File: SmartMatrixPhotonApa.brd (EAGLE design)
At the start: 40.6 x 35.6 mm, 13 parts, among them IC2 74AHC1G08DBV, IC3 74AHC1G08DBV, J1 0-DNP, U1 microSD

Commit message: Rough routing of board, not close to passing DRC
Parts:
- moved C1 7.38 mm to (18.3, 15.0)
- moved JP6 6.97 mm to (20.3, 18.3), turned to 180 degrees
- moved JP8 6.97 mm to (20.3, 18.3)
- moved C2 6.91 mm to (15.7, 18.3), turned to 90 degrees
- moved D1 6.43 mm to (15.2, 11.7)
- moved IC2 6.43 mm to (22.6, 11.4)
- moved IC3 6.43 mm to (18.5, 11.4)
- moved JP3 6.43 mm to (10.4, 0.00)
- moved R2 6.43 mm to (25.7, 11.2)
- moved U1 6.43 mm to (27.6, 20.3)
- moved JP1 6.43 mm to (20.6, 7.62)
- moved J1 5.39 mm to (24.6, 16.5)
- moved R1 4.49 mm to (24.6, 18.5), turned to 0 degrees
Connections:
- net V3.3 renamed 3V3
- new net N$1: JP3.GND@0, JP3.GND@0_1, JP3.GND@0_2, JP3.GND@0_S1, JP3.GND@0_S2
- net GND: now also JP3.GND@2, JP3.GND@2_1, JP3.GND@2_2, JP3.GND@2_S1, JP3.GND@2_S2; no longer JP3.GND@0, JP3.GND@0_1, JP3.GND@0_2, JP3.GND@0_S1, JP3.GND@0_S2
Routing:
- net GND: track 0.00 -> 77.4 mm, vias 0 -> 2
- net VIN: track 0.00 -> 45.6 mm
- net SPI_SCK: track 0.00 -> 26.6 mm, vias 0 -> 1
- net SD_CS: track 0.00 -> 25.9 mm, vias 0 -> 1
- net SPI_MISO: track 0.00 -> 25.4 mm, vias 0 -> 1
- net 3V3: track 0.00 -> 23.9 mm, vias 0 -> 1
- net SPI_MOSI: track 0.00 -> 21.6 mm, vias 0 -> 1
- net N$4: track 0.00 -> 17.0 mm, vias 0 -> 2
- net VEXT: track 0.00 -> 16.1 mm
- net LED_DAT: track 0.00 -> 12.5 mm, vias 0 -> 1
- net LED_CLK: track 0.00 -> 6.82 mm, vias 0 -> 1
- net LED_EN: track 0.00 -> 3.98 mm
- net N$3: track 0.00 -> 3.22 mm
- net N$2: track 0.00 -> 2.59 mm
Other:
- board text added: "Photon SMT Breakout Footprint originally by Particle"
- board text added: "Photon Shield Footprint originally by SparkFun, CC BY-SA 4.0"
- board text added: "Pixelmatix 2016 CC BY-SA 4.0"
- board text added: "Rev V3"
- board text added: "SmartMatrix APA Shield for Photon"

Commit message: Rev V0.1, ready to order prototypes
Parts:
- added D2: MBR0520LT, diode:SOD123
- moved R1 12.2 mm to (24.1, 6.35), turned to 180 degrees
- moved R2 6.82 mm to (20.8, 6.35), turned to 180 degrees
- moved C1 3.34 mm to (15.0, 15.5)
- moved D1 2.97 mm to (14.2, 8.89)
- moved JP6 1.78 mm to (20.3, 16.5)
- moved JP8 1.78 mm to (20.3, 16.5)
- moved IC2 1.70 mm to (23.4, 13.0)
- moved IC3 1.61 mm to (19.1, 13.0)
- moved J1 1.55 mm to (26.2, 16.8)
- moved JP1 1.30 mm to (20.3, 8.89)
- moved C2 0.92 mm to (15.0, 17.8), turned to 0 degrees
- moved U1 0.80 mm to (27.3, 19.6)
- moved JP3 0.25 mm to (10.2, 0.00)
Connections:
- net N$2 renamed CLK
- net N$3 renamed DAT
- removed net N$1: JP3.GND@0, JP3.GND@0_1, JP3.GND@0_2, JP3.GND@0_S1, JP3.GND@0_S2
- net VEXT: now also D2.C
- net VIN: now also D2.A
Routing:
- net 3V3: track 23.9 -> 44.6 mm
- net SPI_MOSI: track 21.6 -> 28.8 mm
- net SPI_MISO: track 25.4 -> 31.9 mm
- net VIN: track 45.6 -> 51.7 mm, vias 0 -> 1
- net SD_CS: track 25.9 -> 31.6 mm
- net GND: track 77.4 -> 82.8 mm, vias 2 -> 4
- net LED_EN: track 3.98 -> 9.13 mm
- net SPI_SCK: track 26.6 -> 31.7 mm
- net LED_CLK: track 6.82 -> 11.8 mm
- net N$4: track 17.0 -> 21.8 mm, vias 2 -> 0
- net LED_DAT: track 12.5 -> 16.5 mm
- net VEXT: track 16.1 -> 14.6 mm
- net CLK: track 2.59 -> 3.11 mm
- added copper zone on layer 1, net GND
- added copper zone on layer 16, net GND
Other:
- board text added: "+5V"
- board text added: "2016-04-26"
- board text added: "CLK"
- board text added: "DAT"
- board text added: "GND"
- board text added: "IC2"
- board text added: "IC3"
- board text added: "Rev V0.1"
- board text added: "SmartMatrix APA102 Shield for Photon"
- board text added: "VEXT"
- board text added: "VIN"
- board text added: "pixl.mx/smkit10"
- board text removed: "Rev V3"
- board text removed: "SmartMatrix APA Shield for Photon"

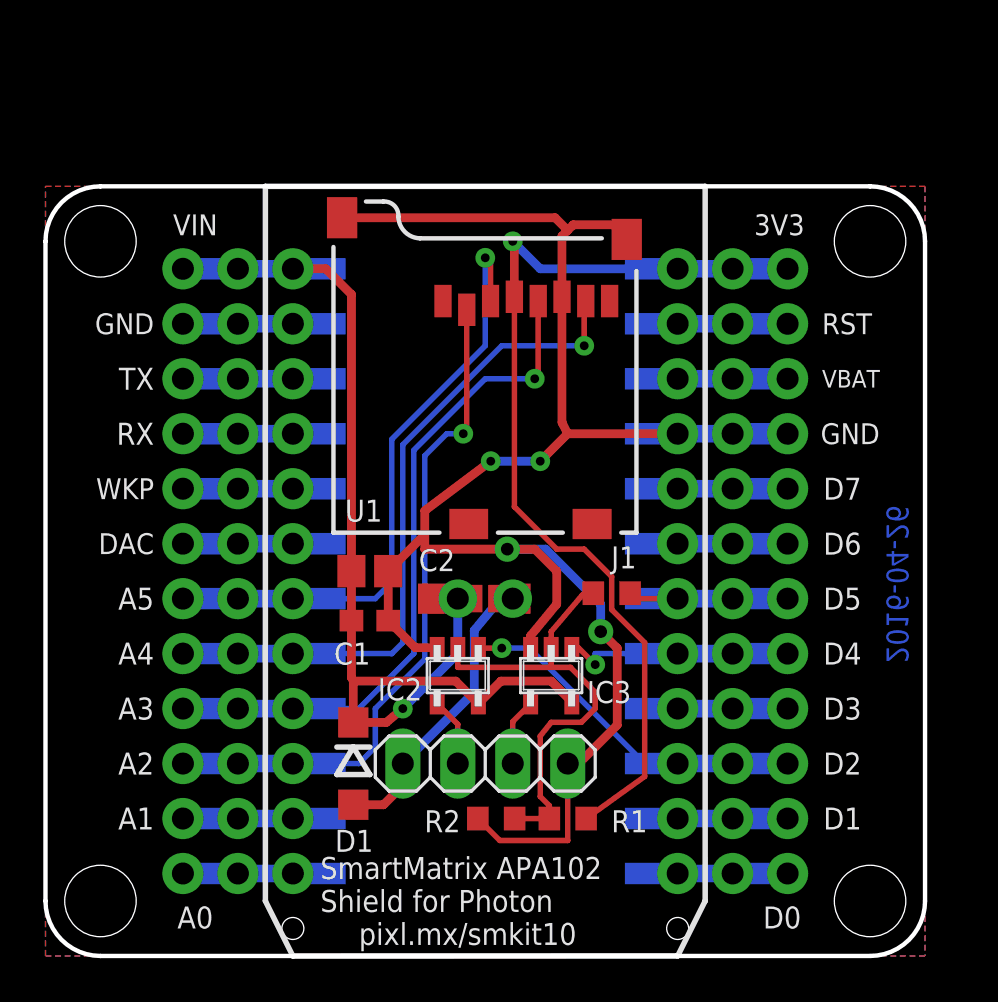
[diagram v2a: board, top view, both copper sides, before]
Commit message: Changes for V1 - Larger holes for APA102 wires - a 1x2 SMT jumper on bottom side of board for VIN and VEXT - optional (DNP) 6.3V 100uF smd 1206 cap to shield to help with USB power kickback when long strip switches - fatter VIN/VEXT to support USB power - photon dual header footprint improvements 	- Make it two parts as the connectors are two separate 2x12 headers 	- Fix the unnecessary DRC errors that show up in Eagle - change to shorter 2x12 connectors - update BOM - label pins used for microSD and apa - Put name on bottom of board (top is covered with Photon)
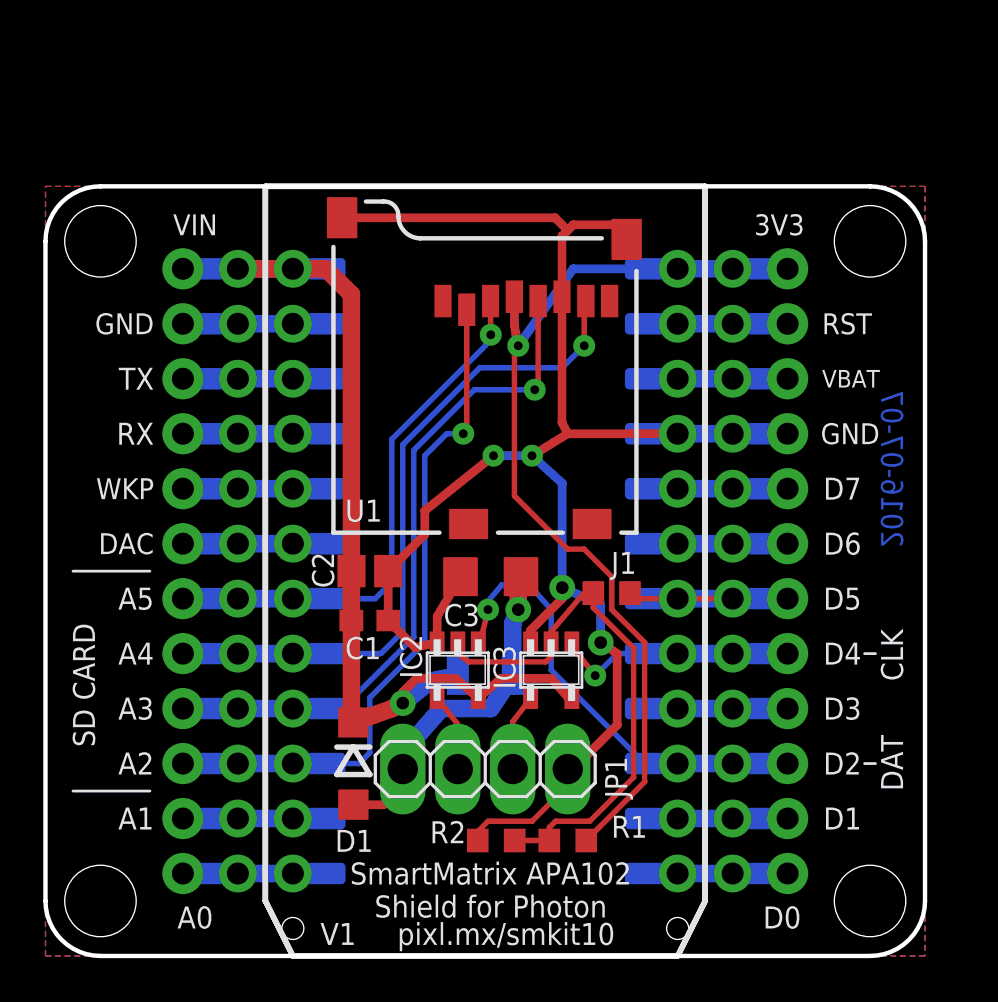
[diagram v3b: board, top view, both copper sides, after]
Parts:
- removed D2: MBR0520LT, diode:SOD123
- removed IC3: 74AHC1G08DBV, 74xx-little-us:SOT23-5
- removed JP6: JUMPER-PTH-2-NO, SparkFun-Passives:PTH-JUMPER-2-NO_NO_SILK
- removed JP8: JUMPER-PAD-2-NO, SparkFun-Passives:PAD-JUMPER-2-NO_NO_SILK
- added C3: 100uF, scanlime:C1206
- added IC1: 74AHC1G08DBV, 74xx-little-us:SOT23-5
- added JP2: (no value), pinhead-2:1X02SMD/90
- added JP4: 2x12 Female SMT Socket, eclibrary:PHOTON_DUAL_HEADER_SHIELD_BOT_MOUNT_RIGHT
- JP1: device pinhead-2:1X04 -> eclibrary:1X04-LARGEHOLE
- JP3: value PARTICLE_PHOTON_TEMPLATES_PIXELMATIX -> 2x12 Female SMT Socket; device eclibrary:PIXELMATIX_PHOTON_SHIELD_TEMPLATE -> eclibrary:PHOTON_DUAL_HEADER_SHIELD_BOT_MOUNT_LEFT
- moved JP3 17.8 mm to (10.2, 17.8), flipped to the bottom
- moved R1 1.02 mm to (24.1, 5.33)
- moved R2 1.02 mm to (20.8, 5.33)
- moved JP1 0.25 mm to (20.3, 8.64)
- moved IC2 0.25 mm to (23.4, 13.2)
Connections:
- new net N$1: JP3.3, JP3.4, JP3.GND@0
- new net N$10: JP4.5, JP4.6, JP4.VBAT
- new net N$11: JP4.10, JP4.9, JP4.D7
- new net N$12: JP4.11, JP4.12, JP4.D6
- new net N$13: JP4.17, JP4.18, JP4.D3
- new net N$14: JP4.21, JP4.22, JP4.D1
- new net N$15: JP4.23, JP4.24, JP4.D0
- new net N$2: JP3.5, JP3.6, JP3.TX
- new net N$3: JP3.7, JP3.8, JP3.RX
- new net N$5: JP3.10, JP3.9, JP3.WKP
- new net N$6: JP3.11, JP3.12, JP3.DAC
- new net N$7: JP3.21, JP3.22, JP3.A1
- new net N$8: JP3.23, JP3.24, JP3.A0
- new net N$9: JP4.3, JP4.4, JP4.RST
- net 3V3: now also JP4.1, JP4.2, JP4.3V3; no longer JP3.3V3, JP3.3V3_1, JP3.3V3_2, JP3.3V3_S1, JP3.3V3_S2
- net DAT: now also IC1.4; no longer IC3.4
- net GND: now also C3.2, IC1.3, JP4.7, JP4.8, JP4.GND@2; no longer IC3.3, JP3.GND@2, JP3.GND@2_1, JP3.GND@2_2, JP3.GND@2_S1, JP3.GND@2_S2
- net LED_CLK: now also JP4.15, JP4.16, JP4.D4; no longer JP3.D4, JP3.D4_1, JP3.D4_2, JP3.D4_S1, JP3.D4_S2
- net LED_DAT: now also IC1.1, JP4.19, JP4.20, JP4.D2; no longer IC3.1, JP3.D2, JP3.D2_1, JP3.D2_2, JP3.D2_S1, JP3.D2_S2
- net LED_EN: now also JP4.13, JP4.14, JP4.D5; no longer JP3.D5, JP3.D5_1, JP3.D5_2, JP3.D5_S1, JP3.D5_S2
- net N$4: now also IC1.2; no longer IC3.2
- net SD_CS: now also JP3.19, JP3.20; no longer JP3.A2_1, JP3.A2_2, JP3.A2_S1, JP3.A2_S2
- net SPI_MISO: now also JP3.15, JP3.16; no longer JP3.A4_1, JP3.A4_2, JP3.A4_S1, JP3.A4_S2
- net SPI_MOSI: now also JP3.13, JP3.14; no longer JP3.A5_1, JP3.A5_2, JP3.A5_S1, JP3.A5_S2
- net SPI_SCK: now also JP3.17, JP3.18; no longer JP3.A3_1, JP3.A3_2, JP3.A3_S1, JP3.A3_S2
- net VEXT: now also C3.1, JP2.1; no longer D2.C, JP6.1, JP8.2
- net VIN: now also IC1.5, JP2.2, JP3.1, JP3.2; no longer D2.A, IC3.5, JP3.VIN1, JP3.VIN2, JP3.VIN_S1, JP3.VIN_S2, JP6.2, JP8.1
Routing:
- net GND: track 82.8 -> 75.5 mm
- net VIN: track 51.7 -> 45.9 mm
- net LED_DAT: track 16.5 -> 21.8 mm
- net N$8: track 0.00 -> 5.08 mm
- net N$7: track 0.00 -> 5.08 mm
- net N$6: track 0.00 -> 5.08 mm
- net N$5: track 0.00 -> 5.08 mm
- net N$3: track 0.00 -> 5.08 mm
- net N$2: track 0.00 -> 5.08 mm
- net N$1: track 0.00 -> 5.08 mm
- net N$9: track 0.00 -> 5.08 mm
- net N$15: track 0.00 -> 5.08 mm
- net N$14: track 0.00 -> 5.08 mm
- net N$13: track 0.00 -> 5.08 mm
- net N$12: track 0.00 -> 5.08 mm
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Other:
- outline, holes or cut-outs redrawn
- board text added: "2016-07-07"
- board text added: "Rev V1"
- board text added: "SD CARD"
- board text added: "V1"
- board text added: "VUSB"
- board text removed: "2016-04-26"
- board text removed: "Rev V0.1"
- board text removed: "VEXT"
- board text removed: "VIN"
